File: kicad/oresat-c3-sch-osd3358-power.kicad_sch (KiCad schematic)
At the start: 37 parts, among them Q6 MMBT2907, U1 OSD3358-512M-BSM, U10 SN74LVC1G07DCK, U14 TLVH431

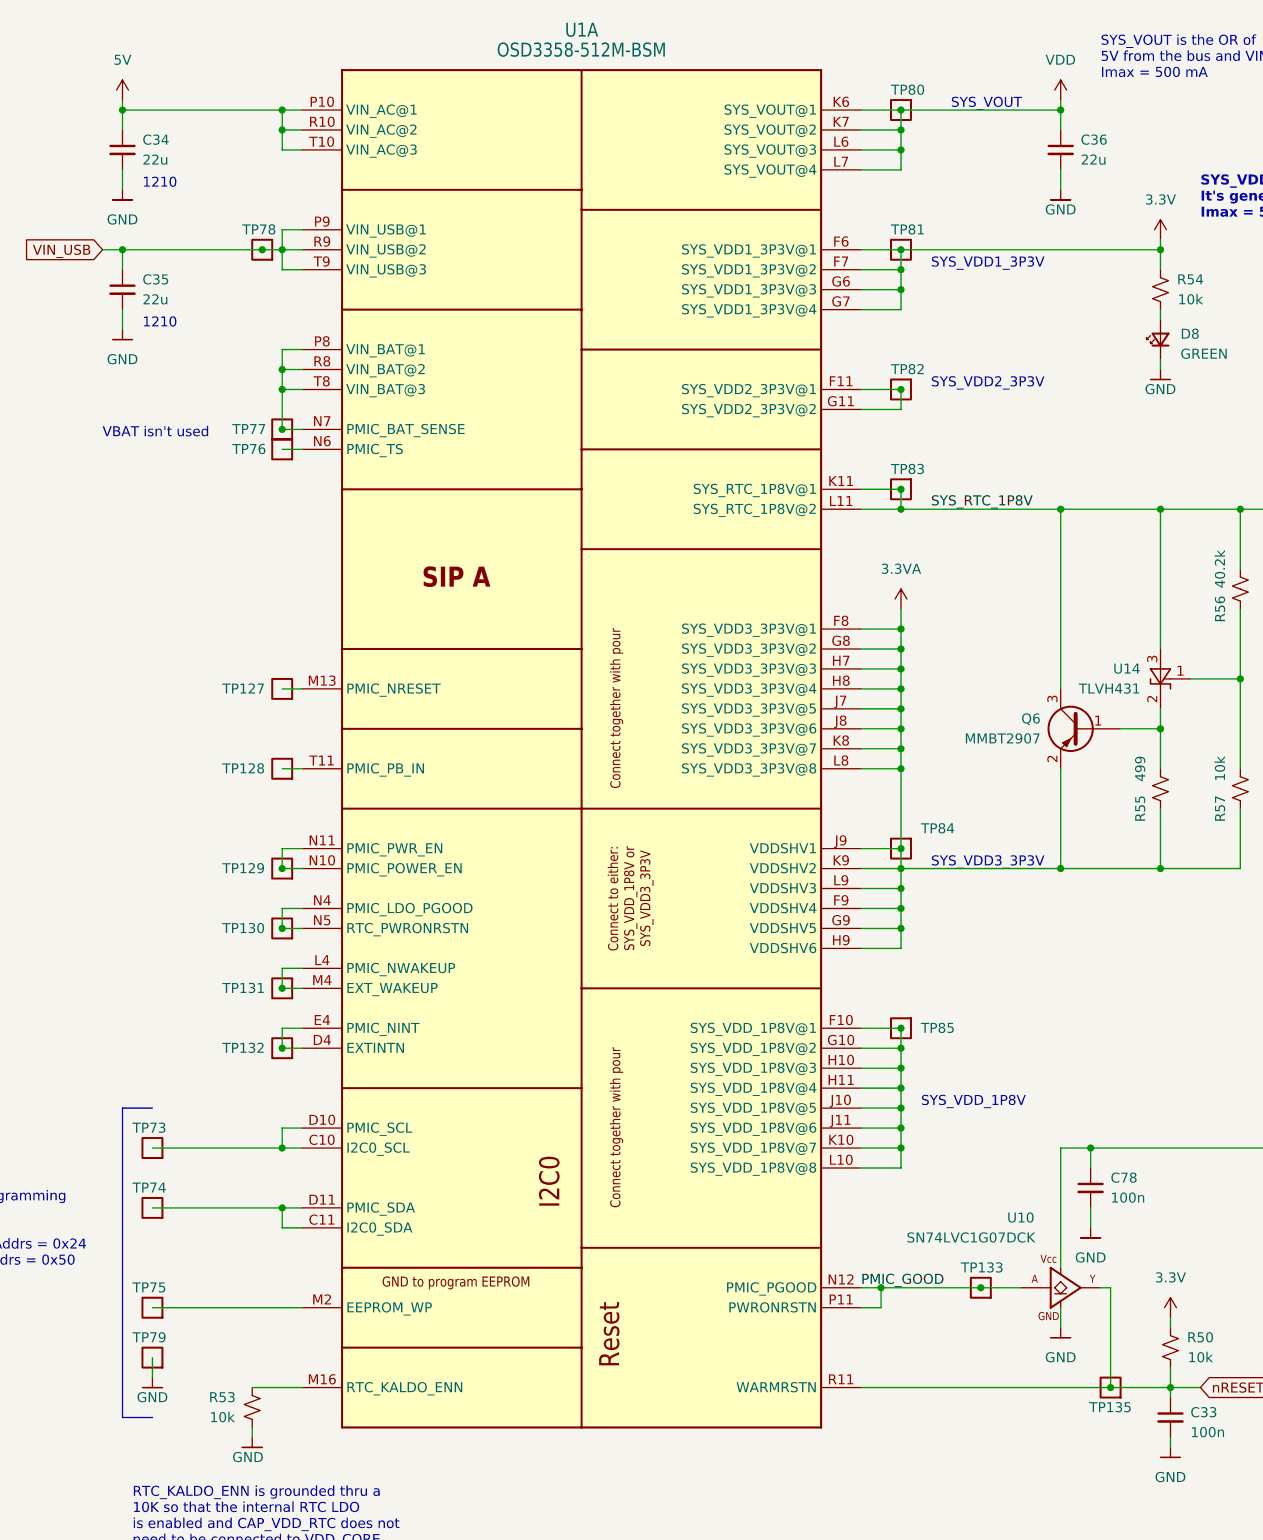
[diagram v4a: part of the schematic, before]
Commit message: Sane amount of ERC errors now; mostly library cleanups.
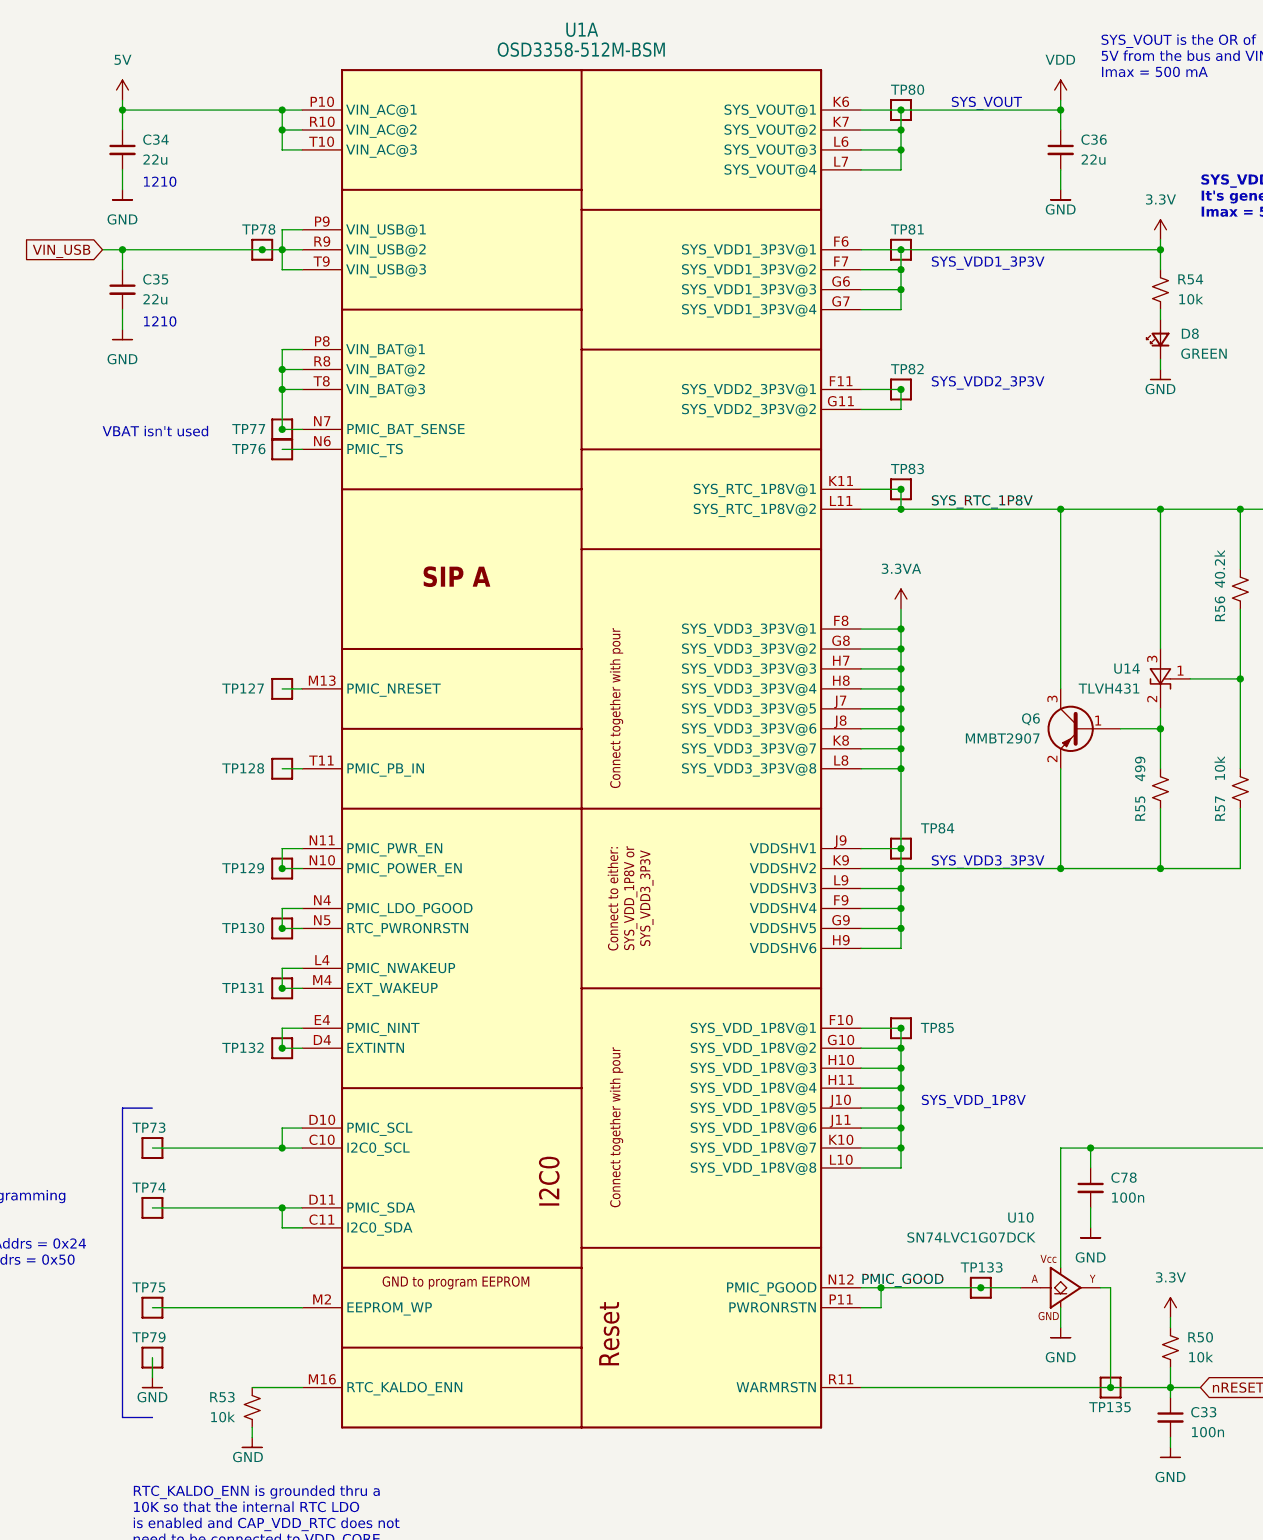
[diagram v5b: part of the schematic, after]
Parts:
- TP127, TP128, TP129, TP130, TP131, TP132, TP133, TP135, TP73, TP74, TP75, TP76, TP77, TP78, TP79, TP80, TP81, TP82, TP83, TP84, TP85: footprint OreSat-TestPoint:PAD.03X.04 -> oresat-misc:PAD.03X.04; symbol OreSat-TestPoint:Test-Point -> oresat-misc:Test-Point
- U10: symbol U-TI-SN74LVC1G07DCK:SN74LVC1G07DCK -> oresat-ics:SN74LVC1G07DCK
- U14: footprint oresat-footprints:SOT23 -> Package_TO_SOT_SMD:SOT-23; symbol U-TI-TLVH431-shunt-regulator:TLVH431 -> oresat-ics:TLVH431
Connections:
- net VDD renamed 1.1V

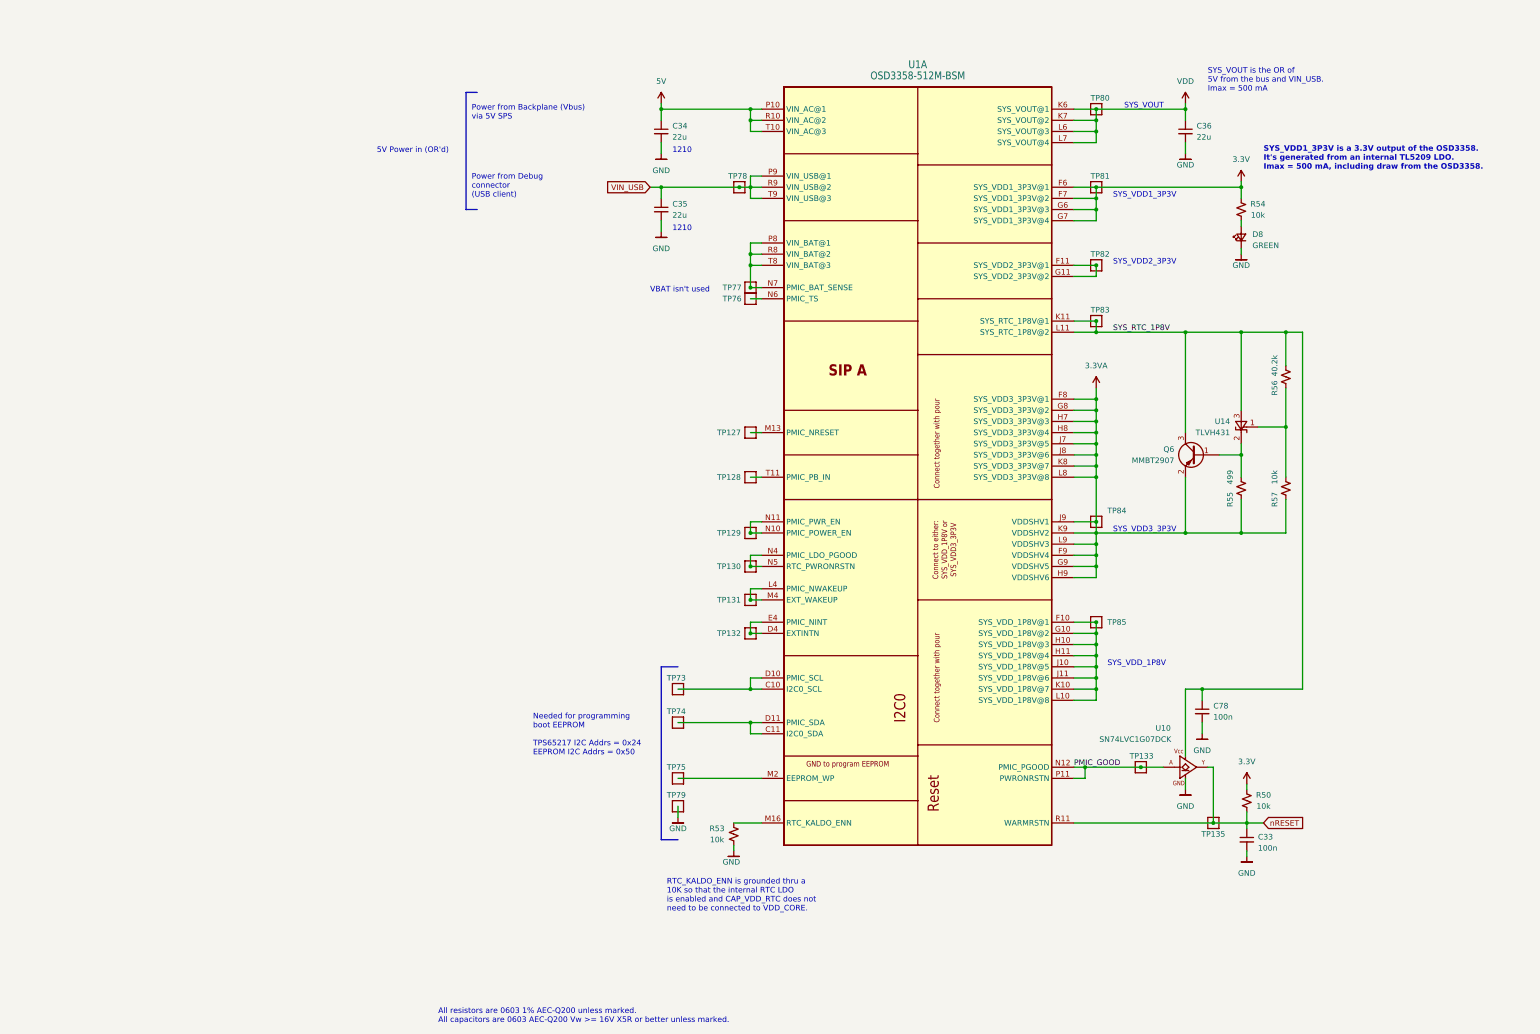
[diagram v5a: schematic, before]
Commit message: Big C3 cleanup with Glenn; radios off of one SPS + separate LDOs, removed lots of test 0 ohm resistors, cleaned up capacitance, and finally wired everything up to the octavo. ZERO ERC errors.
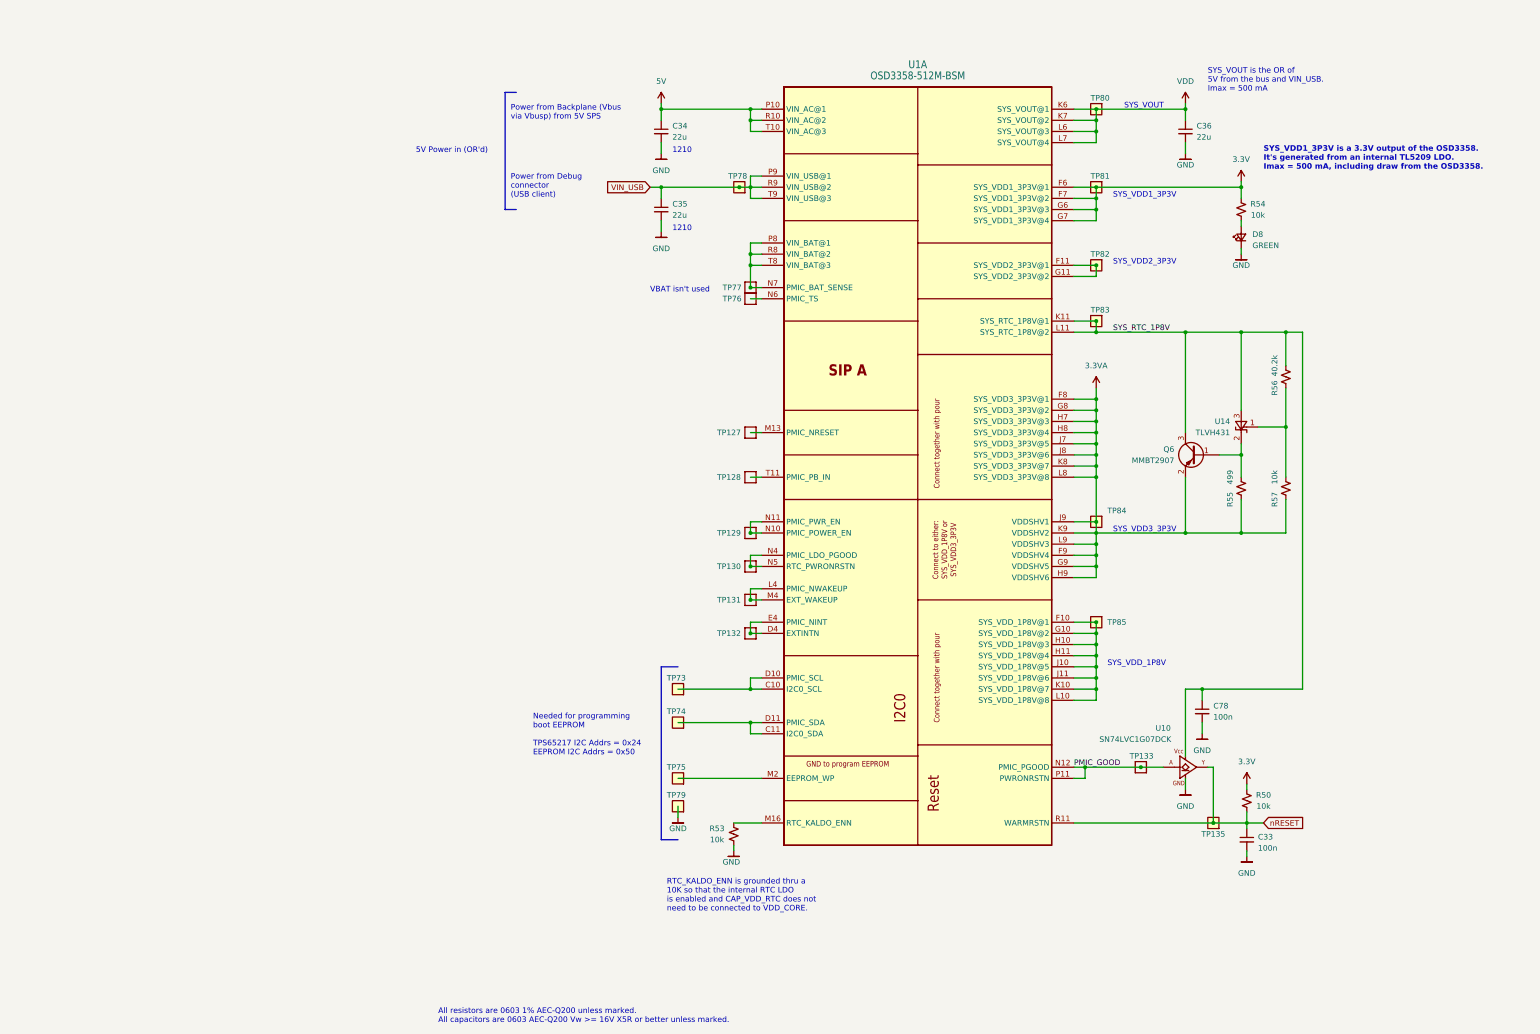
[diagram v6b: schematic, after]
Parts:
- TP127, TP128, TP129, TP130, TP131, TP132, TP133, TP76, TP77: footprint oresat-misc:PAD.03X.04 -> TestPoint:TestPoint_Pad_D1.0mm; symbol oresat-misc:Test-Point -> oresat-misc:Test-Point-1mm-round
- TP135, TP73, TP74, TP75, TP78, TP79, TP80, TP81, TP82, TP83, TP84, TP85: footprint oresat-misc:PAD.03X.04 -> TestPoint:TestPoint_Pad_D1.0mm; symbol oresat-misc:Test-Point -> oresat-misc:Test-Point-0.75mm-th
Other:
- note added: "Power from Backplane (Vbus via Vbusp) from 5V SPS"
- note removed: "Power from Backplane (Vbus) via 5V SPS"

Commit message: Fixed test points; added RF test points. Started on layout and component packages for UHF radio.
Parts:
- TP127, TP128, TP129, TP130, TP131, TP132, TP133, TP76, TP77: footprint TestPoint:TestPoint_Pad_D1.0mm -> oresat-misc:TestPoint_Pad_D1.0mm
- TP135, TP73, TP74, TP75, TP78, TP79, TP80, TP81, TP82, TP83, TP84, TP85: footprint TestPoint:TestPoint_Pad_D1.0mm -> oresat-misc:TestPoint-0.75mm-th
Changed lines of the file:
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@@
       (effects (font (size 1.27 1.27)) hide)
     )
-    (property "Footprint" "TestPoint:TestPoint_Pad_D1.0mm" (at 275.59 147.32 0)
+    (property "Footprint" "oresat-misc:TestPoint-0.75mm-th" (at 275.59 147.32 0)
       (effects (font (size 1.27 1.27)) hide)
     )
@@
       (effects (font (size 1.27 1.27)) hide)
     )
-    (property "Footprint" "TestPoint:TestPoint_Pad_D1.0mm" (at 275.59 170.18 0)
+    (property "Footprint" "oresat-misc:TestPoint-0.75mm-th" (at 275.59 170.18 0)
       (effects (font (size 1.27 1.27)) hide)
     )
@@
       (effects (font (size 1.27 1.27)) hide)
     )
-    (property "Footprint" "TestPoint:TestPoint_Pad_D1.0mm" (at 170.18 215.9 0)
+    (property "Footprint" "oresat-misc:TestPoint-0.75mm-th" (at 170.18 215.9 0)
       (effects (font (size 1.27 1.27)) hide)
     )
@@
       (effects (font (size 1.27 1.27)) hide)
     )
-    (property "Footprint" "TestPoint:TestPoint_Pad_D1.0mm" (at 186.69 160.02 0)
+    (property "Footprint" "oresat-misc:TestPoint_Pad_D1.0mm" (at 186.69 160.02 0)
       (effects (font (size 1.27 1.27)) hide)
     )
@@
       (effects (font (size 1.27 1.27)) hide)
     )
-    (property "Footprint" "TestPoint:TestPoint_Pad_D1.0mm" (at 292.1 226.06 0)
+    (property "Footprint" "oresat-misc:TestPoint-0.75mm-th" (at 292.1 226.06 0)
       (effects (font (size 1.27 1.27)) hide)
     )
@@
       (effects (font (size 1.27 1.27)) hide)
     )
-    (property "Footprint" "TestPoint:TestPoint_Pad_D1.0mm" (at 275.59 71.12 0)
+    (property "Footprint" "oresat-misc:TestPoint-0.75mm-th" (at 275.59 71.12 0)
       (effects (font (size 1.27 1.27)) hide)
     )
@@
       (effects (font (size 1.27 1.27)) hide)
     )
-    (property "Footprint" "TestPoint:TestPoint_Pad_D1.0mm" (at 186.69 182.88 0)
+    (property "Footprint" "oresat-misc:TestPoint_Pad_D1.0mm" (at 186.69 182.88 0)
       (effects (font (size 1.27 1.27)) hide)
     )
@@
       (effects (font (size 1.27 1.27)) hide)
     )
-    (property "Footprint" "TestPoint:TestPoint_Pad_D1.0mm" (at 184.15 81.28 0)
+    (property "Footprint" "oresat-misc:TestPoint-0.75mm-th" (at 184.15 81.28 0)
       (effects (font (size 1.27 1.27)) hide)
     )
@@
       (effects (font (size 1.27 1.27)) hide)
     )
-    (property "Footprint" "TestPoint:TestPoint_Pad_D1.0mm" (at 170.18 222.25 0)
+    (property "Footprint" "oresat-misc:TestPoint-0.75mm-th" (at 170.18 222.25 0)
       (effects (font (size 1.27 1.27)) hide)
     )
@@
       (effects (font (size 1.27 1.27)) hide)
     )
-    (property "Footprint" "TestPoint:TestPoint_Pad_D1.0mm" (at 170.18 203.2 0)
+    (property "Footprint" "oresat-misc:TestPoint-0.75mm-th" (at 170.18 203.2 0)
       (effects (font (size 1.27 1.27)) hide)
     )
@@
       (effects (font (size 1.27 1.27)) hide)
     )
-    (property "Footprint" "TestPoint:TestPoint_Pad_D1.0mm" (at 186.69 167.64 0)
+    (property "Footprint" "oresat-misc:TestPoint_Pad_D1.0mm" (at 186.69 167.64 0)
       (effects (font (size 1.27 1.27)) hide)
     )
@@
       (effects (font (size 1.27 1.27)) hide)
     )
-    (property "Footprint" "TestPoint:TestPoint_Pad_D1.0mm" (at 275.59 53.34 0)
+    (property "Footprint" "oresat-misc:TestPoint-0.75mm-th" (at 275.59 53.34 0)
       (effects (font (size 1.27 1.27)) hide)
     )
@@
       (effects (font (size 1.27 1.27)) hide)
     )
-    (property "Footprint" "TestPoint:TestPoint_Pad_D1.0mm" (at 170.18 195.58 0)
+    (property "Footprint" "oresat-misc:TestPoint-0.75mm-th" (at 170.18 195.58 0)
       (effects (font (size 1.27 1.27)) hide)
     )
@@
       (effects (font (size 1.27 1.27)) hide)
     )
-    (property "Footprint" "TestPoint:TestPoint_Pad_D1.0mm" (at 275.59 101.6 0)
+    (property "Footprint" "oresat-misc:TestPoint-0.75mm-th" (at 275.59 101.6 0)
       (effects (font (size 1.27 1.27)) hide)
     )
@@
       (effects (font (size 1.27 1.27)) hide)
     )
-    (property "Footprint" "TestPoint:TestPoint_Pad_D1.0mm" (at 186.69 147.32 0)
+    (property "Footprint" "oresat-misc:TestPoint_Pad_D1.0mm" (at 186.69 147.32 0)
       (effects (font (size 1.27 1.27)) hide)
     )
@@
       (effects (font (size 1.27 1.27)) hide)
     )
-    (property "Footprint" "TestPoint:TestPoint_Pad_D1.0mm" (at 275.59 88.9 0)
+    (property "Footprint" "oresat-misc:TestPoint-0.75mm-th" (at 275.59 88.9 0)
       (effects (font (size 1.27 1.27)) hide)
     )
@@
       (effects (font (size 1.27 1.27)) hide)
     )
-    (property "Footprint" "TestPoint:TestPoint_Pad_D1.0mm" (at 186.69 137.16 0)
+    (property "Footprint" "oresat-misc:TestPoint_Pad_D1.0mm" (at 186.69 137.16 0)
       (effects (font (size 1.27 1.27)) hide)
     )
@@
       (effects (font (size 1.27 1.27)) hide)
     )
-    (property "Footprint" "TestPoint:TestPoint_Pad_D1.0mm" (at 186.69 106.68 0)
+    (property "Footprint" "oresat-misc:TestPoint_Pad_D1.0mm" (at 186.69 106.68 0)
       (effects (font (size 1.27 1.27)) hide)
     )
@@
       (effects (font (size 1.27 1.27)) hide)
     )
-    (property "Footprint" "TestPoint:TestPoint_Pad_D1.0mm" (at 186.69 104.14 0)
+    (property "Footprint" "oresat-misc:TestPoint_Pad_D1.0mm" (at 186.69 104.14 0)
       (effects (font (size 1.27 1.27)) hide)
     )
@@
       (effects (font (size 1.27 1.27)) hide)
     )
-    (property "Footprint" "TestPoint:TestPoint_Pad_D1.0mm" (at 275.59 213.36 0)
+    (property "Footprint" "oresat-misc:TestPoint_Pad_D1.0mm" (at 275.59 213.36 0)
       (effects (font (size 1.27 1.27)) hide)
     )
@@
       (effects (font (size 1.27 1.27)) hide)
     )
-    (property "Footprint" "TestPoint:TestPoint_Pad_D1.0mm" (at 186.69 175.26 0)
-      (effects (font (size 1.27 1.27)) hide)
-    )
+    (property "Footprint" "oresat-misc:TestPoint_Pad_D1.0mm" (at 186.69 175.26 0)
+      (effects (font (size 1.27 1.27)) hide)
+    )
